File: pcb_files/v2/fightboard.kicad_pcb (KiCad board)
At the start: 2 copper layers, 179 x 60 mm, 56 parts, among them M1 XIAO-RP2040

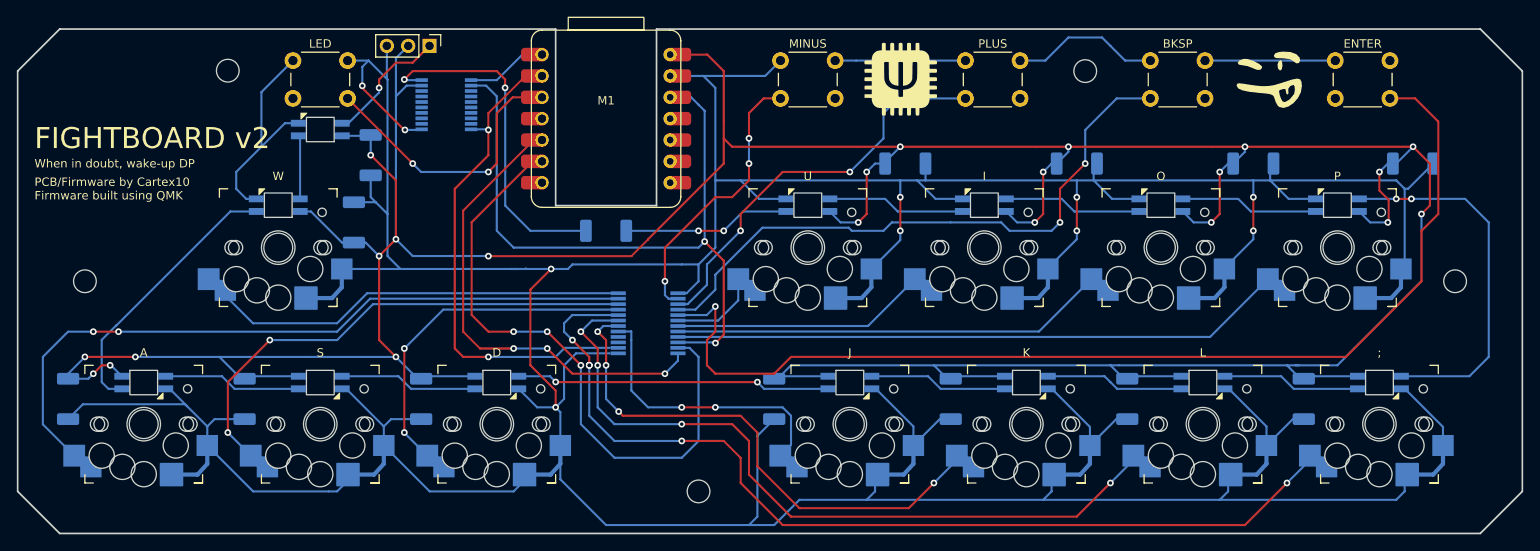
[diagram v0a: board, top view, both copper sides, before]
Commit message: remove capacitors
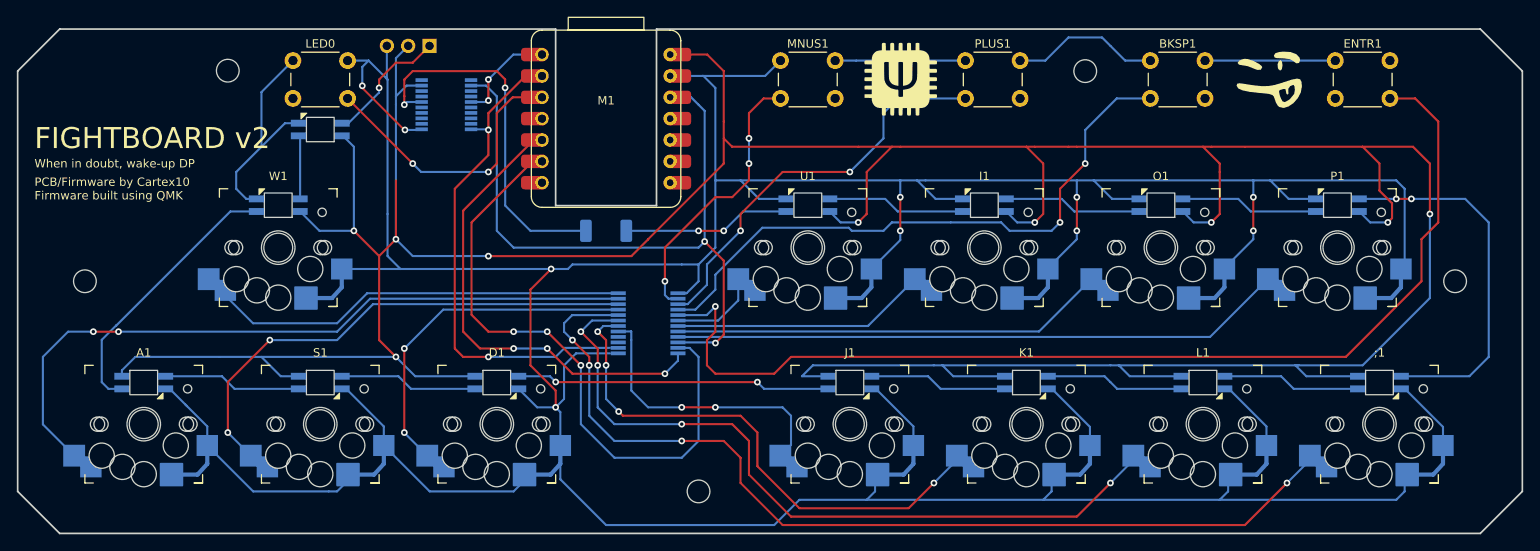
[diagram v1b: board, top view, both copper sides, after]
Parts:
- removed C1, C10, C11, C12, C13, C2, C3, C4, C5, C6, C7, C8, C9: C_Small, Resistor_SMD:R_2010_5025Metric_Pad1.40x2.65mm_HandSolder
- renumbered ; to ;1, A to A1, BKSP to BKSP1, D to D1, ENTER to ENTR1, I to I1, J to J1, K to K1, L to L1, LED to LED0, MINUS to MNUS1, O to O1, P to P1, PLUS to PLUS1, S to S1, U to U1, W to W1
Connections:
- LED13 pad 2: unconnected-(LED13-Pad2) -> unconnected-(LED13-DOUT-Pad2)
- LS1 pad 1: Net-(M1-Pad1) -> unconnected-(LS1-A1-Pad1)
- LS1 pad 16: unconnected-(LS1-Pad16) -> Net-(LS1-B4)
- LS1 pad 20: Net-(R330-Pad2) -> unconnected-(LS1-B1-Pad20)
- LS1 pad 5: unconnected-(LS1-Pad5) -> Net-(LS1-A4)
- M1 pad 1: Net-(M1-Pad1) -> Net-(LS1-A4)
- R330 pad 2: Net-(R330-Pad2) -> Net-(LS1-B4)
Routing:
- net Net-(IOEX1-ADDR): track 686.2 -> 610.8 mm
- net Net-(LS1-B4): track 0.00 -> 43.9 mm, vias 0 -> 2
- net Net-(R330-Pad2): track 40.8 -> 0.00 mm, vias 2 -> 0
- net Net-(LED1-VDD): track 481.9 -> 450.7 mm, vias 22 -> 9
- net Net-(LS1-A4): track 0.00 -> 12.4 mm, vias 0 -> 2
- net Net-(M1-Pad1): track 9.70 -> 0.00 mm
- net Net-(IOEX1-GPA3): vias 5 -> 4
